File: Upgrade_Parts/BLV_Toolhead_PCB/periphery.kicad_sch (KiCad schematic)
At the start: 14 parts

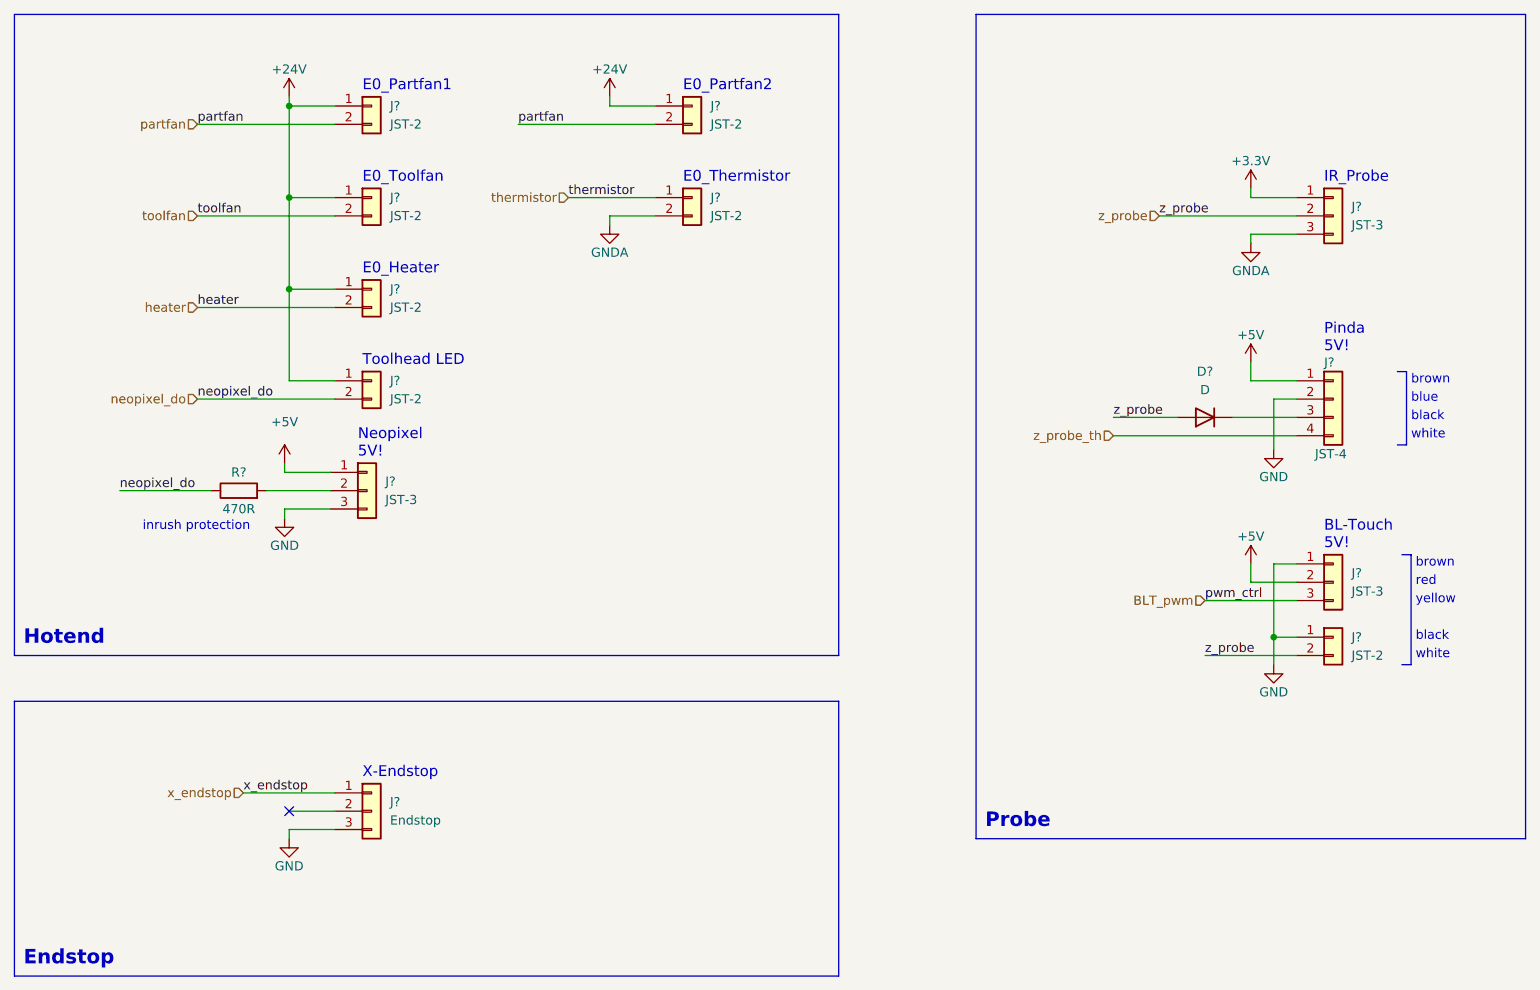
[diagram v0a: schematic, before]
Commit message: removed lvds drivers
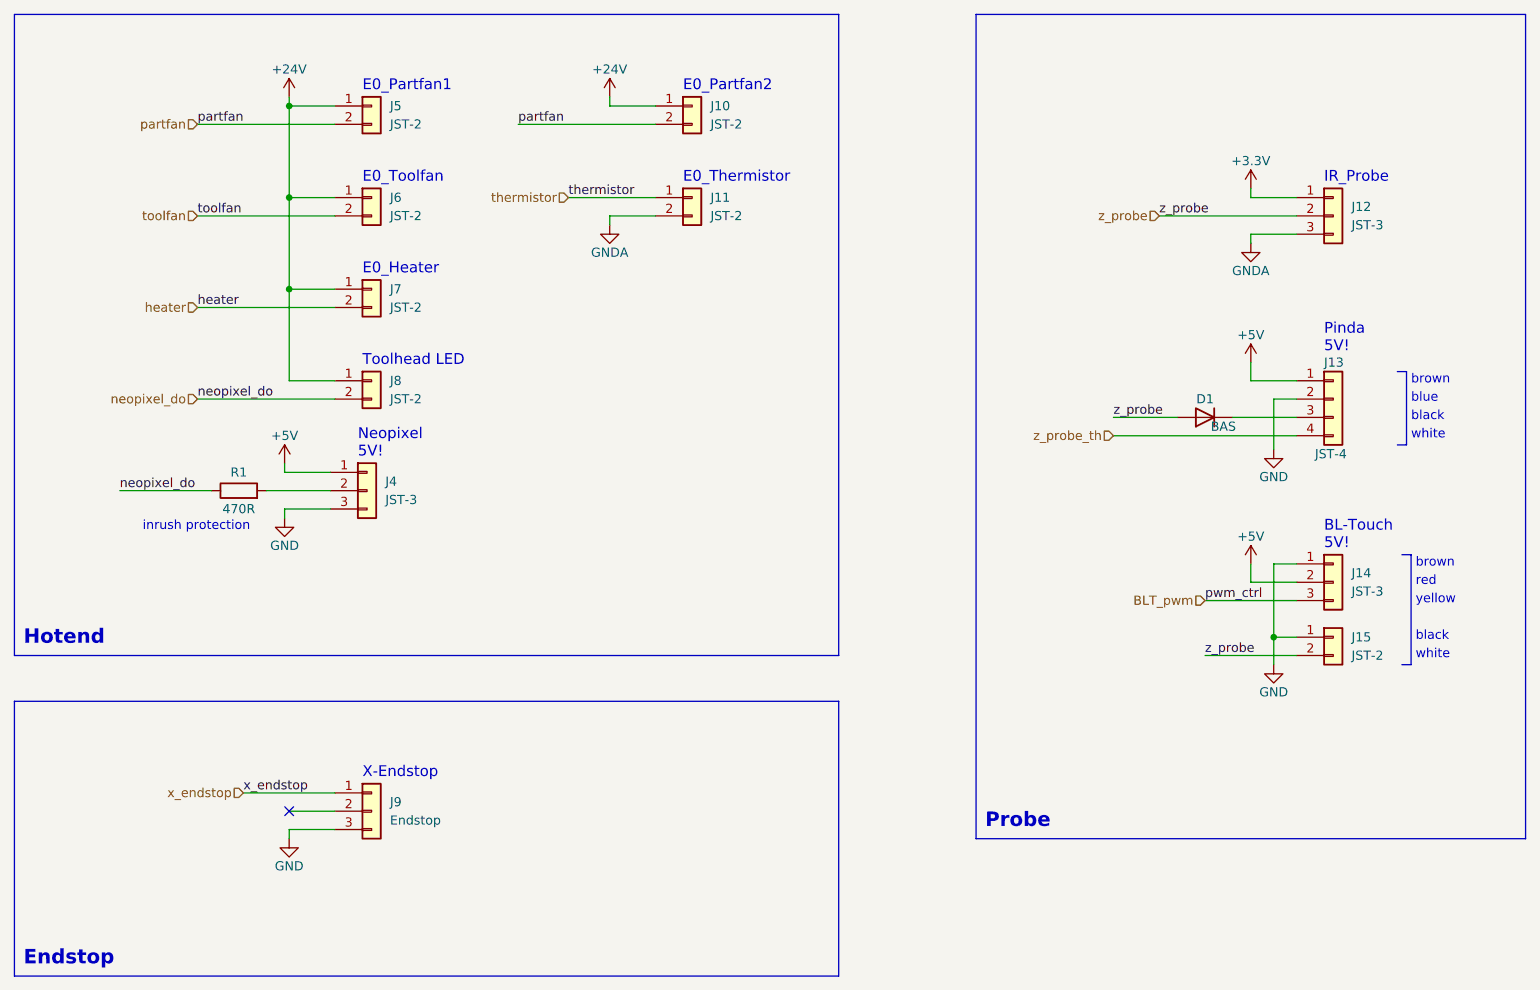
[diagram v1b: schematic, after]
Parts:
- D1: renamed from D?; value D -> BAS; footprint (none) -> Diode_SMD:D_0603_1608Metric
- R1: renamed from R?; footprint (none) -> Resistor_SMD:R_0603_1608Metric
- gave numbers to parts that had none: 12
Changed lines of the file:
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@@
   (symbol (lib_id "Connector_Generic:Conn_01x02") (at 93.98 44.45 0) (unit 1)
     (in_bom yes) (on_board yes) (fields_autoplaced)
-    (property "Reference" "J?" (id 0) (at 96.52 44.4499 0)
+    (property "Reference" "J5" (id 0) (at 96.52 44.4499 0)
       (effects (font (size 1.27 1.27)) (justify left))
     )
@@
   (symbol (lib_id "Connector_Generic:Conn_01x02") (at 93.98 69.85 0) (unit 1)
     (in_bom yes) (on_board yes) (fields_autoplaced)
-    (property "Reference" "J?" (id 0) (at 96.52 69.8499 0)
+    (property "Reference" "J7" (id 0) (at 96.52 69.8499 0)
       (effects (font (size 1.27 1.27)) (justify left))
     )
@@
   )
   (symbol (lib_id "power:+5V") (at 81.915 93.98 0) (unit 1)
-    (in_bom yes) (on_board yes) (fields_autoplaced)
-    (property "Reference" "#PWR?" (id 0) (at 81.915 97.79 0)
-      (effects (font (size 1.27 1.27)) hide)
-    )
-    (property "Value" "+5V" (id 1) (at 81.915 88.265 0))
+    (in_bom yes) (on_board yes)
+    (property "Reference" "#PWR018" (id 0) (at 81.915 97.79 0)
+      (effects (font (size 1.27 1.27)) hide)
+    )
+    (property "Value" "+5V" (id 1) (at 81.915 90.17 0))
     (property "Footprint" "" (id 2) (at 81.915 93.98 0)
       (effects (font (size 1.27 1.27)) hide)
@@
   (symbol (lib_id "Connector_Generic:Conn_01x04") (at 227.33 85.09 0) (unit 1)
     (in_bom yes) (on_board yes)
-    (property "Reference" "J?" (id 0) (at 226.06 80.01 0)
+    (property "Reference" "J13" (id 0) (at 226.06 80.01 0)
       (effects (font (size 1.27 1.27)) (justify left))
     )
@@
   (symbol (lib_id "Connector_Generic:Conn_01x03") (at 227.33 110.49 0) (unit 1)
     (in_bom yes) (on_board yes) (fields_autoplaced)
-    (property "Reference" "J?" (id 0) (at 229.87 109.2199 0)
+    (property "Reference" "J14" (id 0) (at 229.87 109.2199 0)
       (effects (font (size 1.27 1.27)) (justify left))
     )
@@
   (symbol (lib_id "power:GND") (at 81.915 101.6 0) (unit 1)
     (in_bom yes) (on_board yes)
-    (property "Reference" "#PWR?" (id 0) (at 81.915 107.95 0)
+    (property "Reference" "#PWR019" (id 0) (at 81.915 107.95 0)
       (effects (font (size 1.27 1.27)) hide)
     )
@@
   (symbol (lib_id "power:+5V") (at 215.9 80.01 0) (unit 1)
     (in_bom yes) (on_board yes)
-    (property "Reference" "#PWR?" (id 0) (at 215.9 83.82 0)
+    (property "Reference" "#PWR026" (id 0) (at 215.9 83.82 0)
       (effects (font (size 1.27 1.27)) hide)
     )
@@
   (symbol (lib_id "power:GNDA") (at 215.9 63.5 0) (unit 1)
     (in_bom yes) (on_board yes)
-    (property "Reference" "#PWR?" (id 0) (at 215.9 69.85 0)
+    (property "Reference" "#PWR025" (id 0) (at 215.9 69.85 0)
       (effects (font (size 1.27 1.27)) hide)
     )
@@
   (symbol (lib_id "power:+3.3V") (at 215.9 55.88 0) (unit 1)
     (in_bom yes) (on_board yes)
-    (property "Reference" "#PWR?" (id 0) (at 215.9 59.69 0)
+    (property "Reference" "#PWR024" (id 0) (at 215.9 59.69 0)
       (effects (font (size 1.27 1.27)) hide)
     )
@@
   (symbol (lib_id "Device:R") (at 75.565 97.79 90) (unit 1)
     (in_bom yes) (on_board yes)
-    (property "Reference" "R?" (id 0) (at 75.565 95.25 90))
+    (property "Reference" "R1" (id 0) (at 75.565 95.25 90))
     (property "Value" "470R" (id 1) (at 75.565 100.33 90))
-    (property "Footprint" "" (id 2) (at 75.565 99.568 90)
+    (property "Footprint" "Resistor_SMD:R_0603_1608Metric" (id 2) (at 75.565 99.568 90)
       (effects (font (size 1.27 1.27)) hide)
     )
@@
   (symbol (lib_id "power:GND") (at 219.075 121.92 0) (unit 1)
     (in_bom yes) (on_board yes)
-    (property "Reference" "#PWR?" (id 0) (at 219.075 128.27 0)
+    (property "Reference" "#PWR029" (id 0) (at 219.075 128.27 0)
       (effects (font (size 1.27 1.27)) hide)
     )
@@
   )
   (symbol (lib_id "Device:D") (at 209.55 87.63 180) (unit 1)
-    (in_bom yes) (on_board yes) (fields_autoplaced)
-    (property "Reference" "D?" (id 0) (at 209.55 81.28 0))
-    (property "Value" "D" (id 1) (at 209.55 83.82 0))
-    (property "Footprint" "" (id 2) (at 209.55 87.63 0)
+    (in_bom yes) (on_board yes)
+    (property "Reference" "D1" (id 0) (at 209.55 85.09 0))
+    (property "Value" "BAS" (id 1) (at 212.09 88.9 0))
+    (property "Footprint" "Diode_SMD:D_0603_1608Metric" (id 2) (at 209.55 87.63 0)
       (effects (font (size 1.27 1.27)) hide)
     )
@@
   (symbol (lib_id "power:+24V") (at 82.55 43.18 0) (unit 1)
     (in_bom yes) (on_board yes)
-    (property "Reference" "#PWR?" (id 0) (at 82.55 46.99 0)
+    (property "Reference" "#PWR020" (id 0) (at 82.55 46.99 0)
       (effects (font (size 1.27 1.27)) hide)
     )
@@
   (symbol (lib_id "Connector_Generic:Conn_01x02") (at 227.33 118.11 0) (unit 1)
     (in_bom yes) (on_board yes) (fields_autoplaced)
-    (property "Reference" "J?" (id 0) (at 229.87 118.1099 0)
+    (property "Reference" "J15" (id 0) (at 229.87 118.1099 0)
       (effects (font (size 1.27 1.27)) (justify left))
     )
@@
   (symbol (lib_id "power:+24V") (at 127 43.18 0) (unit 1)
     (in_bom yes) (on_board yes)
-    (property "Reference" "#PWR?" (id 0) (at 127 46.99 0)
+    (property "Reference" "#PWR022" (id 0) (at 127 46.99 0)
       (effects (font (size 1.27 1.27)) hide)
     )
@@
   (symbol (lib_id "Connector_Generic:Conn_01x03") (at 93.98 142.24 0) (unit 1)
     (in_bom yes) (on_board yes) (fields_autoplaced)
-    (property "Reference" "J?" (id 0) (at 96.52 140.9699 0)
+    (property "Reference" "J9" (id 0) (at 96.52 140.9699 0)
       (effects (font (size 1.27 1.27)) (justify left))
     )
@@
   (symbol (lib_id "Connector_Generic:Conn_01x02") (at 93.98 57.15 0) (unit 1)
     (in_bom yes) (on_board yes) (fields_autoplaced)
-    (property "Reference" "J?" (id 0) (at 96.52 57.1499 0)
+    (property "Reference" "J6" (id 0) (at 96.52 57.1499 0)
       (effects (font (size 1.27 1.27)) (justify left))
     )
@@
   (symbol (lib_id "Connector_Generic:Conn_01x02") (at 93.98 82.55 0) (unit 1)
     (in_bom yes) (on_board yes) (fields_autoplaced)
-    (property "Reference" "J?" (id 0) (at 96.52 82.5499 0)
+    (property "Reference" "J8" (id 0) (at 96.52 82.5499 0)
       (effects (font (size 1.27 1.27)) (justify left))
     )
@@
   (symbol (lib_id "Connector_Generic:Conn_01x03") (at 227.33 59.69 0) (unit 1)
     (in_bom yes) (on_board yes) (fields_autoplaced)
-    (property "Reference" "J?" (id 0) (at 229.87 58.4199 0)
+    (property "Reference" "J12" (id 0) (at 229.87 58.4199 0)
       (effects (font (size 1.27 1.27)) (justify left))
     )
@@
   (symbol (lib_id "Connector_Generic:Conn_01x02") (at 138.43 57.15 0) (unit 1)
     (in_bom yes) (on_board yes) (fields_autoplaced)
-    (property "Reference" "J?" (id 0) (at 140.97 57.1499 0)
+    (property "Reference" "J11" (id 0) (at 140.97 57.1499 0)
       (effects (font (size 1.27 1.27)) (justify left))
     )
@@
   (symbol (lib_id "power:GND") (at 219.075 92.075 0) (unit 1)
     (in_bom yes) (on_board yes)
-    (property "Reference" "#PWR?" (id 0) (at 219.075 98.425 0)
+    (property "Reference" "#PWR028" (id 0) (at 219.075 98.425 0)
       (effects (font (size 1.27 1.27)) hide)
     )
@@
   (symbol (lib_id "power:GND") (at 82.55 146.05 0) (unit 1)
     (in_bom yes) (on_board yes)
-    (property "Reference" "#PWR?" (id 0) (at 82.55 152.4 0)
+    (property "Reference" "#PWR021" (id 0) (at 82.55 152.4 0)
       (effects (font (size 1.27 1.27)) hide)
     )
@@
   (symbol (lib_id "Connector_Generic:Conn_01x03") (at 93.345 97.79 0) (unit 1)
     (in_bom yes) (on_board yes) (fields_autoplaced)
-    (property "Reference" "J?" (id 0) (at 95.885 96.5199 0)
+    (property "Reference" "J4" (id 0) (at 95.885 96.5199 0)
       (effects (font (size 1.27 1.27)) (justify left))
     )
@@
   (symbol (lib_id "power:+5V") (at 215.9 107.95 0) (unit 1)
     (in_bom yes) (on_board yes)
-    (property "Reference" "#PWR?" (id 0) (at 215.9 111.76 0)
+    (property "Reference" "#PWR027" (id 0) (at 215.9 111.76 0)
       (effects (font (size 1.27 1.27)) hide)
     )
@@
   (symbol (lib_id "Connector_Generic:Conn_01x02") (at 138.43 44.45 0) (unit 1)
     (in_bom yes) (on_board yes) (fields_autoplaced)
-    (property "Reference" "J?" (id 0) (at 140.97 44.4499 0)
+    (property "Reference" "J10" (id 0) (at 140.97 44.4499 0)
       (effects (font (size 1.27 1.27)) (justify left))
     )
@@
   (symbol (lib_id "power:GNDA") (at 127 60.96 0) (unit 1)
     (in_bom yes) (on_board yes)
-    (property "Reference" "#PWR?" (id 0) (at 127 67.31 0)
-      (effects (font (size 1.27 1.27)) hide)
-    )
+    (property "Reference" "#PWR023" (id 0) (at 127 67.31 0)
+      (effects (font (size 1.27 1.27)) hide)
+    )
